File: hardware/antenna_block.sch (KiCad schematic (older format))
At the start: 31 parts, among them P301 BNC, T301 TRANSFO, T302 TRANSFO

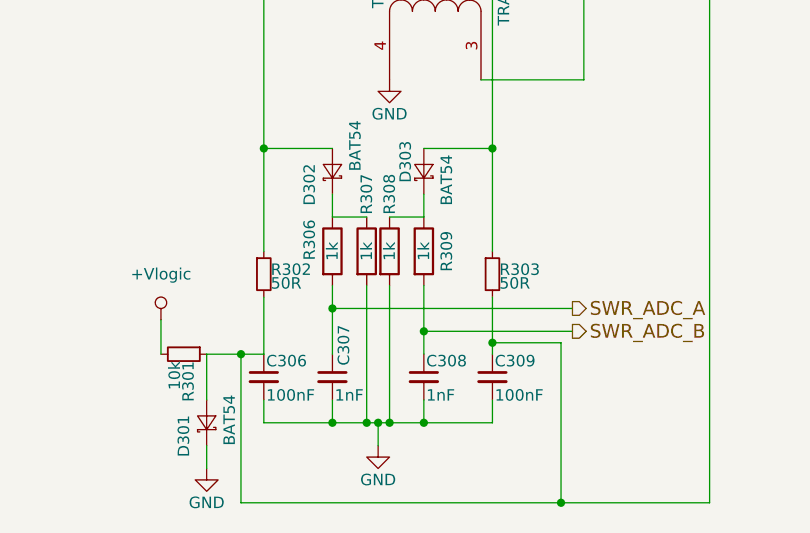
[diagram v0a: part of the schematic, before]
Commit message: changed some component values
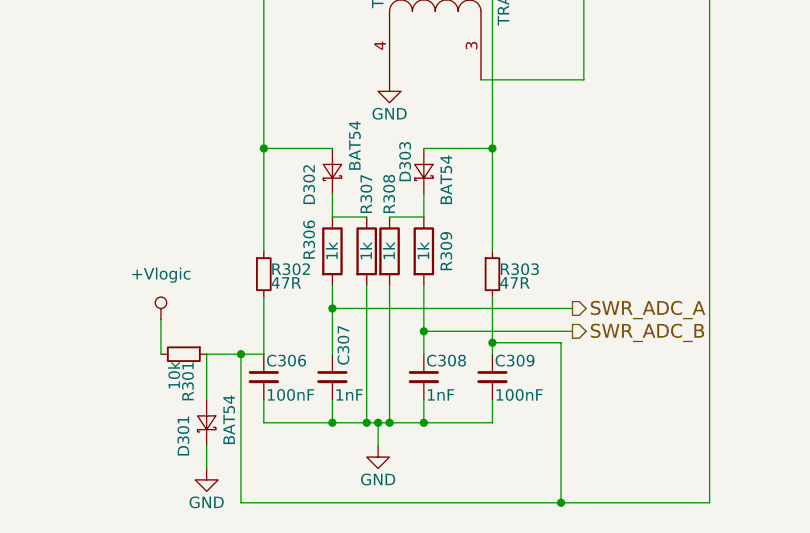
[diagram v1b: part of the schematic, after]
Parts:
- R302, R303: value 50R -> 47R
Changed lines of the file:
@@
 P 4250 5550
 F 0 "R302" H 4280 5570 50  0000 L CNN
-F 1 "50R" H 4280 5510 50  0000 L CNN
+F 1 "47R" H 4280 5510 50  0000 L CNN
 F 2 "Resistors_SMD:R_0805_HandSoldering" H 4250 5550 50  0001 C CNN
 F 3 "" H 4250 5550 50  0000 C CNN
@@
 P 5250 5550
 F 0 "R303" H 5280 5570 50  0000 L CNN
-F 1 "50R" H 5280 5510 50  0000 L CNN
+F 1 "47R" H 5280 5510 50  0000 L CNN
 F 2 "Resistors_SMD:R_0805_HandSoldering" H 5250 5550 50  0001 C CNN
 F 3 "" H 5250 5550 50  0000 C CNN

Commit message: Changed some component values
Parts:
- D301, D302, D303: value BAT54 -> BAT54SL
- D304, D305, D306: value BAP65-02 -> BA891
- R301: value 10k -> 7k87
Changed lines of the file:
@@
 P 3900 5900
 F 0 "R301" H 3930 5920 50  0000 L CNN
-F 1 "10k" H 3930 5860 50  0000 L CNN
+F 1 "7k87" H 3930 5860 50  0000 L CNN
 F 2 "Resistors_SMD:R_0805_HandSoldering" H 3900 5900 50  0001 C CNN
 F 3 "" H 3900 5900 50  0000 C CNN
@@
 P 4000 6200
 F 0 "D301" H 3850 6300 50  0000 L CNN
-F 1 "BAT54" H 3900 6100 50  0000 L CNN
+F 1 "BAT54SL" H 3900 6100 50  0000 L CNN
 F 2 "dodekaedri:SOT-23_HS_2-1-3" V 4000 6200 50  0001 C CNN
 F 3 "" V 4000 6200 50  0000 C CNN
@@
 P 4550 5100
 F 0 "D302" H 4400 5200 50  0000 L CNN
-F 1 "BAT54" H 4550 5000 50  0000 L CNN
+F 1 "BAT54SL" H 4550 5000 50  0000 L CNN
 F 2 "dodekaedri:SOT-23_HS_2-1-3" V 4550 5100 50  0001 C CNN
 F 3 "" V 4550 5100 50  0000 C CNN
@@
 P 4950 5100
 F 0 "D303" H 4900 5180 50  0000 L CNN
-F 1 "BAT54" H 4800 5000 50  0000 L CNN
+F 1 "BAT54SL" H 4800 5000 50  0000 L CNN
 F 2 "dodekaedri:SOT-23_HS_2-1-3" V 4950 5100 50  0001 C CNN
 F 3 "" V 4950 5100 50  0000 C CNN
@@
 P 7200 3600
 F 0 "D304" H 7100 3700 50  0000 L CNN
-F 1 "BAP65-02" H 7050 3520 50  0000 L CNN
+F 1 "BA891" H 7050 3520 50  0000 L CNN
 F 2 "Diodes_SMD:SOD-523" V 7200 3600 50  0001 C CNN
 F 3 "" V 7200 3600 50  0000 C CNN
@@
 P 7450 3100
 F 0 "D305" H 7400 3180 50  0000 L CNN
-F 1 "BAP65-02" H 7300 3020 50  0000 L CNN
+F 1 "BA891" H 7300 3020 50  0000 L CNN
 F 2 "Diodes_SMD:SOD-523" V 7450 3100 50  0001 C CNN
 F 3 "" V 7450 3100 50  0000 C CNN
@@
 P 7450 3600
 F 0 "D306" H 7400 3680 50  0000 L CNN
-F 1 "BAP65-02" H 7300 3520 50  0000 L CNN
+F 1 "BA891" H 7300 3520 50  0000 L CNN
 F 2 "Diodes_SMD:SOD-523" V 7450 3600 50  0001 C CNN
 F 3 "" V 7450 3600 50  0000 C CNN
